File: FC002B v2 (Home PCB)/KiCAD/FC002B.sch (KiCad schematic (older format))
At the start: 53 parts, among them IC1 MSP430G2202, IC10 SC52-11, IC11 SC52-11, IC12 SC52-11, IC2 74HC238, IC3 74HC4060, IC4 74HC4520, IC5 SC52-11, IC6 SC52-11, IC7 SC52-11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

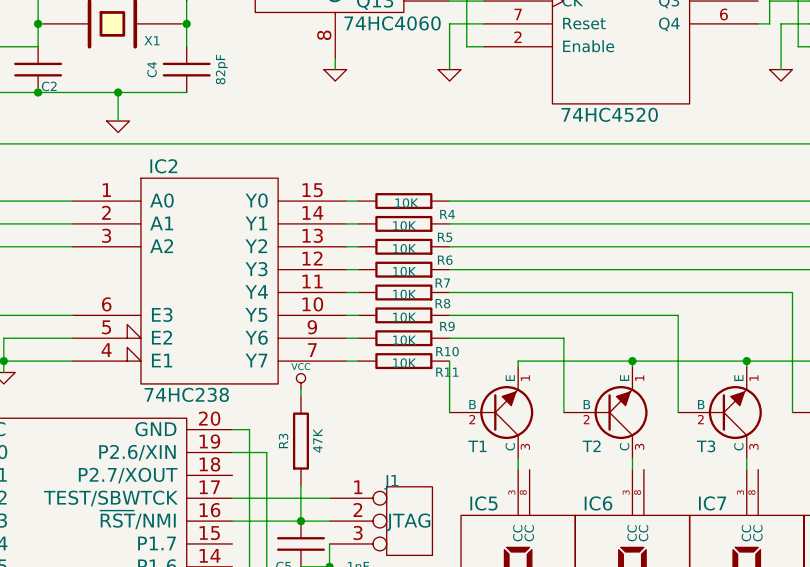
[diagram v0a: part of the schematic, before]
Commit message: Changed the digit driver resistors to 4,7k
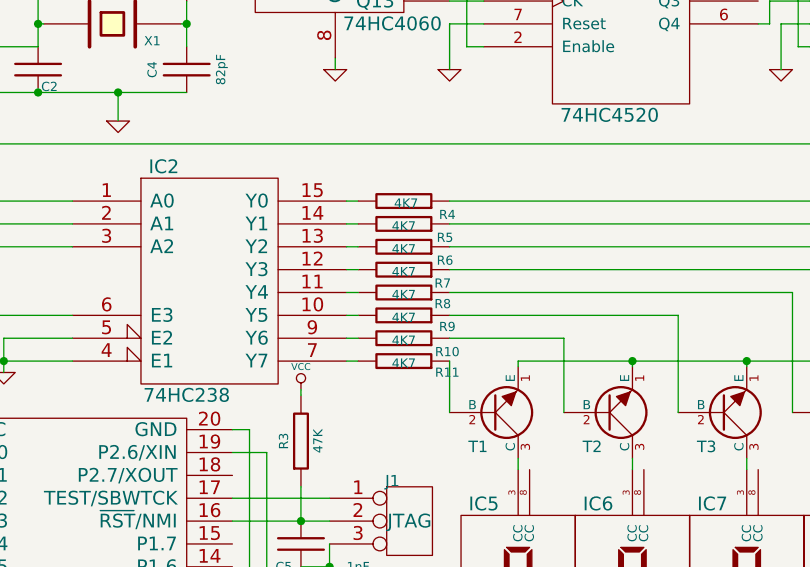
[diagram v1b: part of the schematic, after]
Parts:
- R10, R11, R4, R5, R6, R7, R8, R9: value 10K -> 4K7

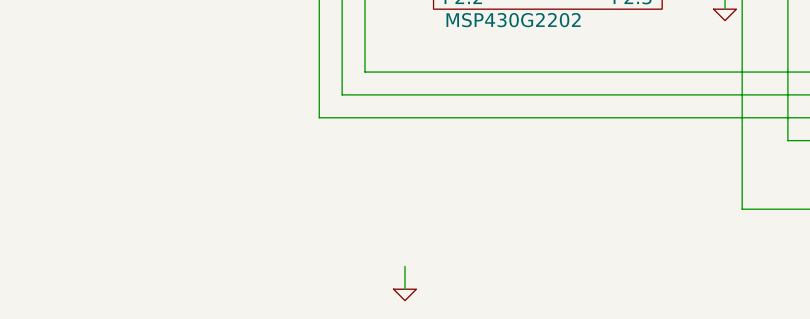
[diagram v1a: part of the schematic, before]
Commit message: Added a new software fork for time period based measurement FC002OPT_G2202+LF
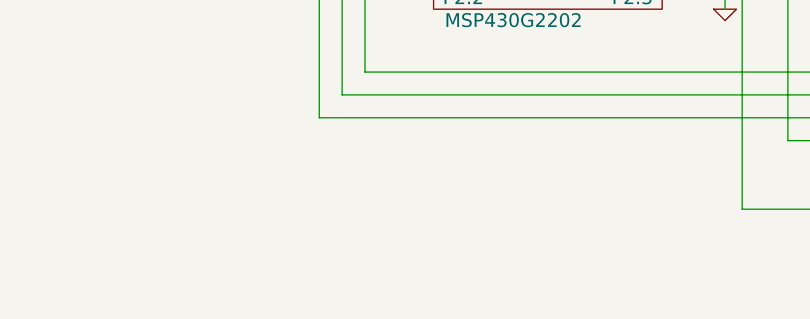
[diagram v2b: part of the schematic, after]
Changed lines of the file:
@@
 Sheet 1 1
 Title ""
-Date "22 aug 2013"
+Date "27 oct 2013"
 Rev ""
 Comp ""
@@
 Wire Wire Line
 	3900 1750 3900 2650
-Wire Wire Line
-	3425 6400 3425 6500
 Connection ~ 3750 4025
 Wire Wire Line
@@
 	1    0    0    -1
 $EndComp
-$Comp
-L GND #PWR017
-U 1 1 5126874F
-P 3425 6500
-F 0 "#PWR017" H 3425 6500 30  0001 C CNN
-F 1 "GND" H 3425 6430 30  0001 C CNN
-F 2 "" H 3425 6500 60  0001 C CNN
-F 3 "" H 3425 6500 60  0001 C CNN
-	1    3425 6500
-	1    0    0    -1
-$EndComp
